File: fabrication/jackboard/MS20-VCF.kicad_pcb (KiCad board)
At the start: 2 copper layers, 60 x 110 mm, 33 parts, among them J1 FilterCV1, J10 Conn_JackBoard, J11 FilterCV2, J12 FilterOut2, J14 Conn_JackBoard, J15 FilterIn2, J2 FilterOut1, J4 Conn_JackBoard, J5 FilterIn1, J7 Conn_JackBoard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

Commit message: update front panel and infos on components
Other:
- board text added: "Double MS-20 VCF V1.3 BleepSound 2023"
- board text removed: "Double MS-20 VCF V1.2 BleepSound 2022"

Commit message: update documentation + update repo layout
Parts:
- CUTCV1, CUTCV2, CUTOFF1, CUTOFF2, Res1, Res2: footprint Synth:Pot-bourns-alpha -> Kicad-perso:Pot-bourns-alpha
- J1, J11, J12, J15, J2, J5: footprint Synth:Thonkiconn -> Kicad-perso:Thonkiconn
- SW1, SW3: footprint Synth:SW_DPDT_Toggle -> Kicad-perso:SW_DPDT_Toggle
- SW2: footprint Synth:SW_Toggle_Blue_wSlots -> Kicad-perso:SW_Toggle_Blue_wSlots

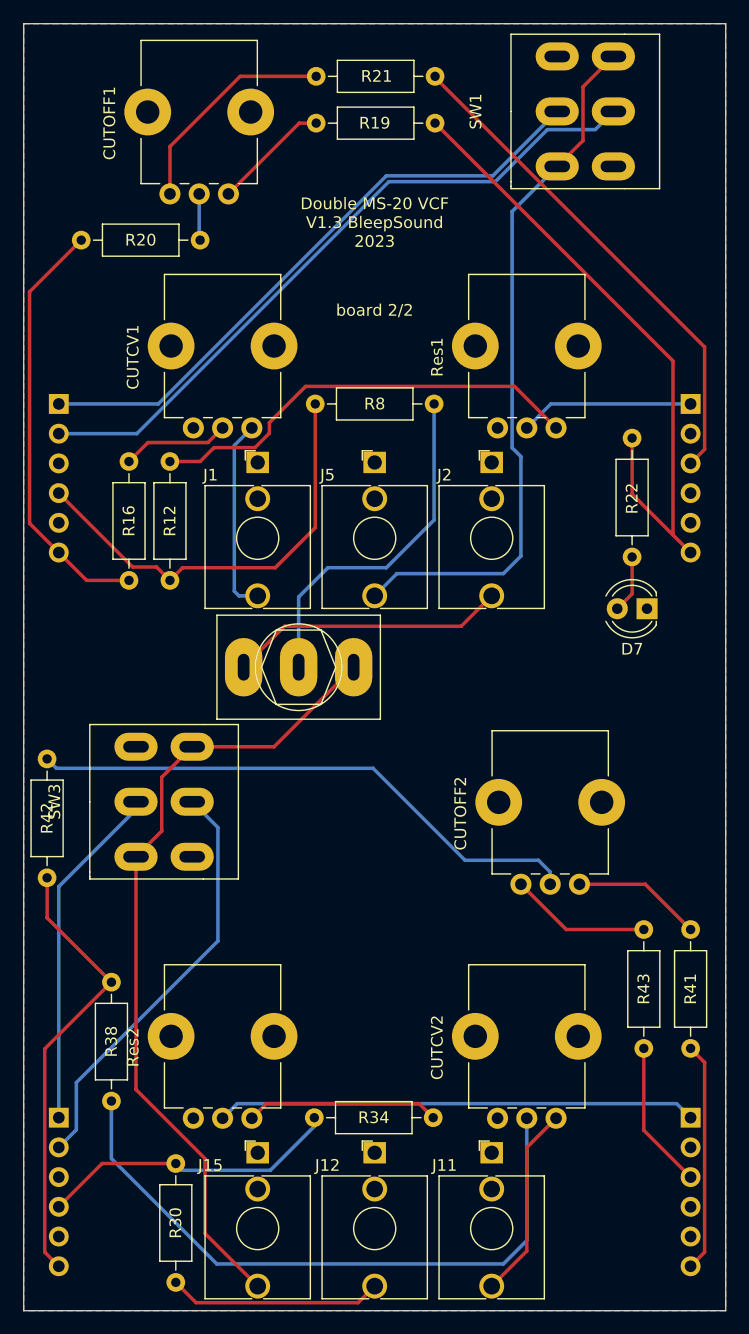
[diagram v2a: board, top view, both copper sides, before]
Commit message: V2.0
new front panel layout
new normalisation for CV and in/out for bandpass filter
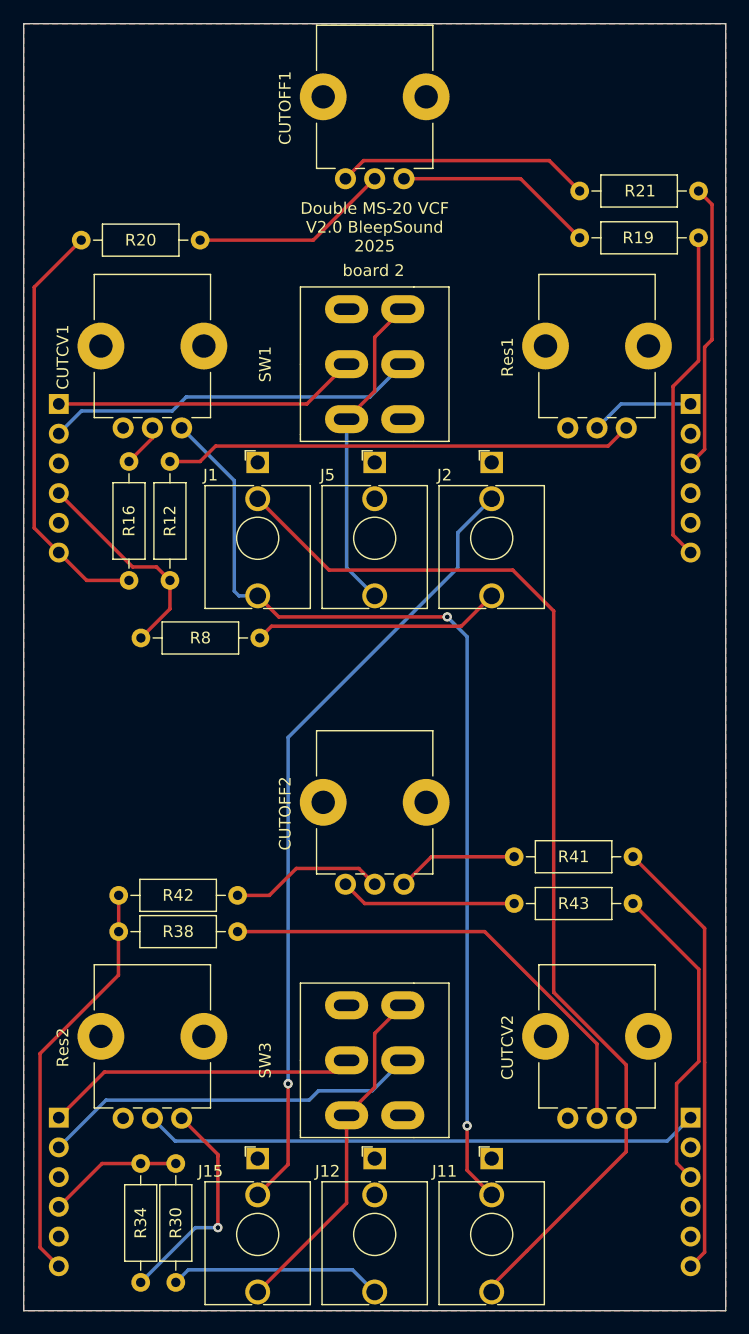
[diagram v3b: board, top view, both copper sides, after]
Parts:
- removed D7: LED-12V, LED_THT:LED_D4.0mm
- removed R22: 2.2k, Resistor_THT:R_Axial_DIN0207_L6.3mm_D2.5mm_P10.16mm_Horizontal
- removed SW2: Bandpass, Kicad-perso:SW_Toggle_Blue_wSlots
- CUTCV1, CUTCV2, CUTOFF1, CUTOFF2, Res1, Res2: value 100k -> B100k
- J1: value FilterCV1 -> jack
- J11: value FilterCV2 -> jack
- J12: value FilterOut2 -> jack
- J15: value FilterIn2 -> jack
- J2: value FilterOut1 -> jack
- J5: value FilterIn1 -> jack
- moved R34 28.7 mm to (105.0, 144.1), turned to 90 degrees
- moved SW3 28.5 mm to (125.0, 125.1)
- moved SW1 28.1 mm to (125.0, 65.6)
- moved R8 24.9 mm to (115.2, 89.0)
- moved R19 24.6 mm to (142.5, 54.8)
- moved R21 24.6 mm to (152.7, 50.8)
- moved R41 16.3 mm to (136.9, 107.7), turned to 0 degrees
- moved CUTOFF1 15.1 mm to (127.5, 49.8)
- moved CUTOFF2 15.0 mm to (127.5, 110.0)
- moved R43 12.4 mm to (147.1, 111.7), turned to 180 degrees
- moved R42 6.30 mm to (103.1, 111.0), turned to 0 degrees
- moved CUTCV1 6.00 mm to (108.5, 71.0)
- moved CUTCV2 6.00 mm to (146.5, 130.1)
- moved Res1 6.00 mm to (146.5, 71.0)
- moved Res2 6.00 mm to (108.5, 130.1)
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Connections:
- CUTCV1 pad 1: /CVIn -> GND
- CUTCV1 pad 3: GND -> CV1In
- CUTCV2 pad 1: /Filtre2/CVIn -> GND
- CUTCV2 pad 3: GND -> CV2In
- J1 pad T: /CVIn -> CV1In
- J1 pad TN: unconnected-(J1-PadTN) -> CV2In
- J11 pad T: /Filtre2/CVIn -> CV2In
- J11 pad TN: unconnected-(J11-PadTN) -> CV1In
- J15 pad T: Filter2In -> /Filtre2/FilterIn
- J15 pad TN: unconnected-(J15-PadTN) -> Filter2In
- J2 pad T: /JackOut -> /FilterOut
- J2 pad TN: unconnected-(J2-PadTN) -> Filter2In
- R19 pad 1: Net-(CUTOFF1-Pad1) -> Net-(CUTOFF1-Pad3)
- R21 pad 2: Net-(CUTOFF1-Pad3) -> Net-(CUTOFF1-Pad1)
- R41 pad 1: Net-(CUTOFF2-Pad1) -> Net-(CUTOFF2-Pad3)
- R43 pad 2: Net-(CUTOFF2-Pad3) -> Net-(CUTOFF2-Pad1)
- Res1 pad 1: Net-(R12-Pad1) -> GND
- Res1 pad 3: GND -> Net-(R12-Pad1)
- Res2 pad 1: Net-(R34-Pad1) -> GND
- Res2 pad 3: GND -> Net-(R34-Pad1)
- SW3 pad 3: Filter2In -> /Filtre2/FilterIn
- SW3 pad 4: Filter2In -> /Filtre2/FilterIn
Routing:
- net CV2In: track 0.00 -> 94.3 mm
- net CV1In: track 0.00 -> 85.9 mm, vias 0 -> 2
- net Net-(CUTOFF2-Pad2): track 48.1 -> 13.2 mm
- net /FilterIn: track 60.5 -> 27.5 mm
- net /Filtre2/FilterIn: track 0.00 -> 29.6 mm
- net /LPass: track 53.0 -> 26.0 mm
- net /HPass: track 58.8 -> 31.9 mm
- net /JackOut: track 23.7 -> 0.00 mm
- net /Out1: track 37.5 -> 18.5 mm
- net /CVIn: track 16.7 -> 0.00 mm
- net /Filtre2/CVIn: track 16.6 -> 0.00 mm
- net Net-(CUTCV2-Pad2): track 55.4 -> 41.0 mm
- net /Filtre2/Out1: track 25.9 -> 11.5 mm
- net Net-(CUTOFF1-Pad2): track 4.10 -> 17.3 mm
- net Net-(CUTOFF1-Pad1): track 10.0 -> 21.7 mm
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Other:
- board text added: "Double MS-20 VCF V2.0 BleepSound 2025"
- board text added: "board 2"
- board text removed: "Double MS-20 VCF V1.3 BleepSound 2023"
- board text removed: "board 2/2"
